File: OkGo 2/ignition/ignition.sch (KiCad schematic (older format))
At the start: 42 parts, among them P101 JST_XH_F, P102 JST_XH_M, P103 CHARGE_CASE, P104 BATT, P105 BATT, P106 SMA, P107 ARM_LED, P108 ARM_LED, SW101 20A ROCKER, U101 CLIP, U102 FUSE 15A, U103 SWD, U104 BEZEL, U105 RFM95W, U106 STM32F071CBT6, U107 TSR 0.5-2433, Y101 8MHz

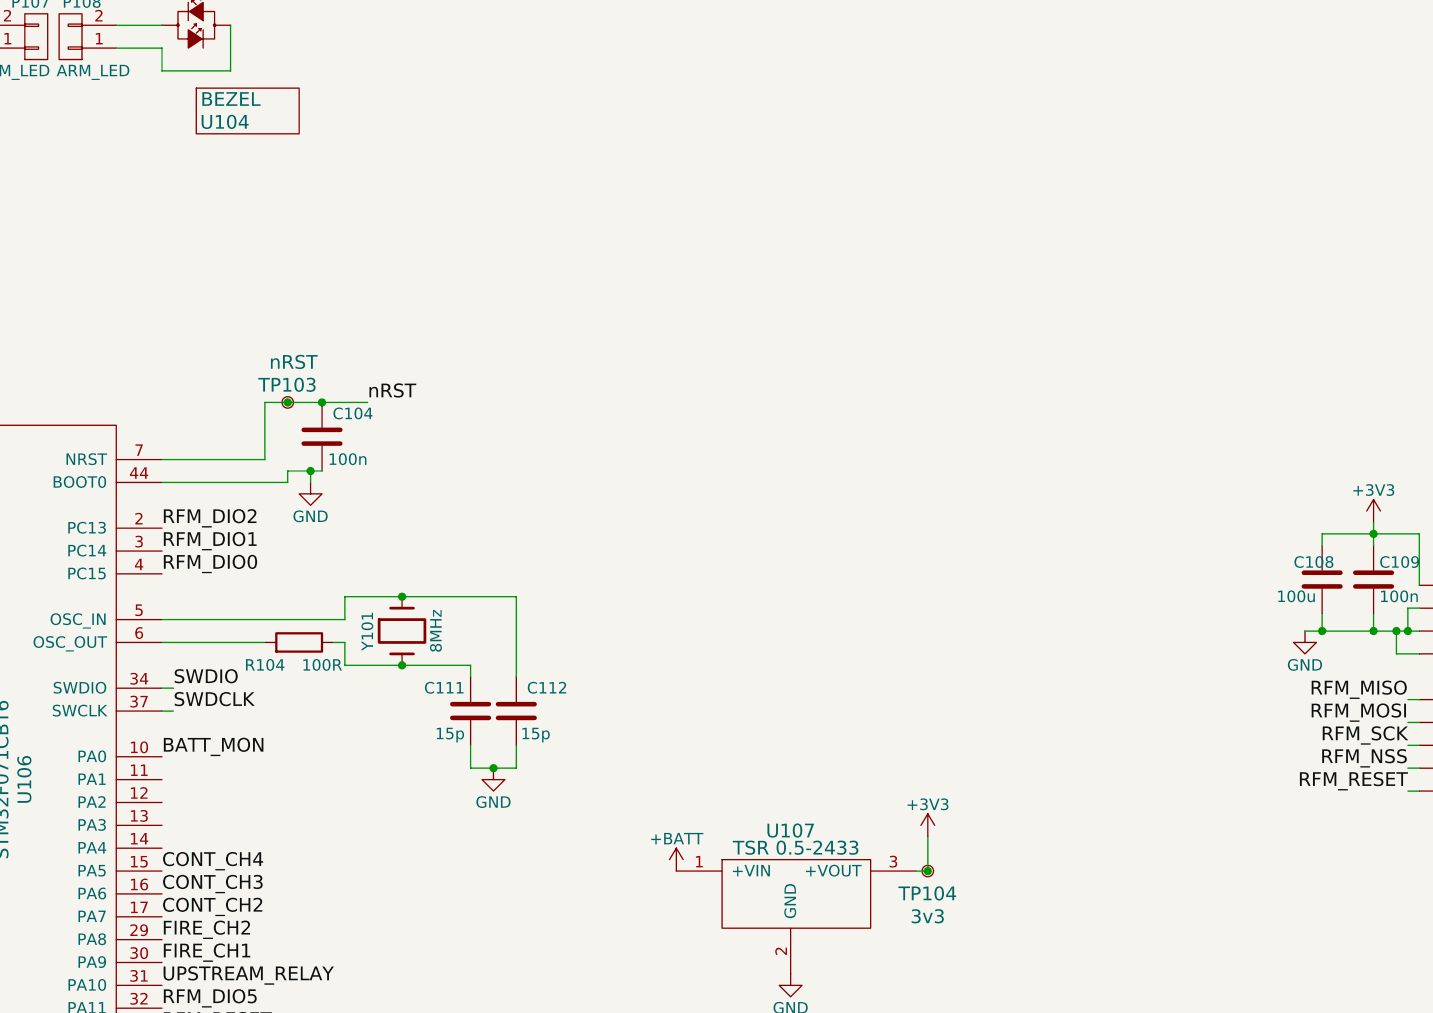
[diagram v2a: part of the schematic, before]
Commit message: Fixed #28, fixed #24, general tidying
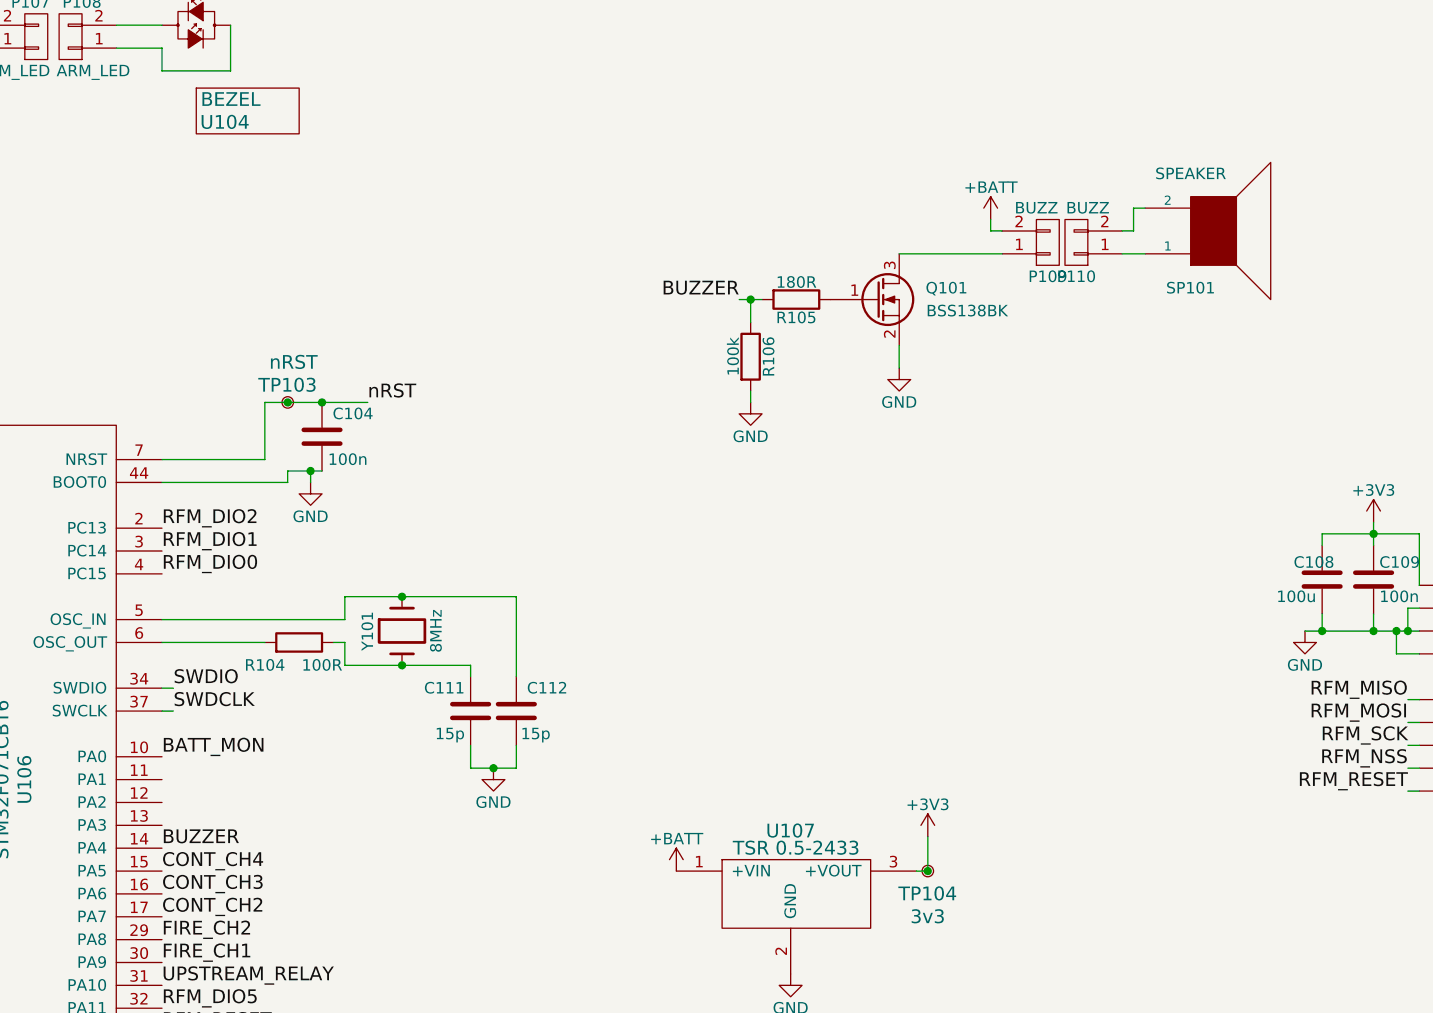
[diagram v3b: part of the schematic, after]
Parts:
- added P109: BUZZ, ignition:JST-PA-2-VERT, symbol CONN_01X02
- added P110: BUZZ, symbol CONN_01X02
- added Q101: BSS138BK, Housings_SOT-23_SOT-143_TSOT-6:SOT-23, symbol Q_NMOS_GSD
- added R105: 180R, Resistors_SMD:R_0805, symbol R
- added R106: 100k, Resistors_SMD:R_0805, symbol R
- added SP101: SPEAKER, symbol SPEAKER
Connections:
- net +BATT: now also P109.2 (P2)
- net GND: now also Q101.2 (S), R106.2
- net BUZZER: now reaches U106.14 (PA4)
- net BUZZER: now also R105.2, R106.1
- new net: P110.1 (P1), SP101.1
- new net: P110.2 (P2), SP101.2
- new net: P109.1 (P1), Q101.3 (D)
- new net: Q101.1 (G), R105.1
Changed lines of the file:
@@
 Wire Wire Line
 	3300 2900 3600 2900
+Text Label 3300 6300 0    60   ~ 0
+BUZZER
+Text Label 5825 3900 2    60   ~ 0
+BUZZER
+$Comp
+L SPEAKER SP101
+U 1 1 55CE427E
+P 7900 3600
+F 0 "SP101" H 7800 3850 50  0000 C CNN
+F 1 "SPEAKER" H 7800 3350 50  0000 C CNN
+F 2 "" H 7900 3600 60  0000 C CNN
+F 3 "http://www.farnell.com/datasheets/1838539.pdf" H 7900 3600 60  0001 C CNN
+F 4 "2433030" H 7900 3600 60  0001 C CNN "Farnell"
+	1    7900 3600
+	1    0    0    1
+$EndComp
+$Comp
+L CONN_01X02 P110
+U 1 1 55CE4BD3
+P 7300 3650
+F 0 "P110" H 7300 3800 50  0000 C CNN
+F 1 "BUZZ" H 7250 3500 50  0000 C CNN
+F 2 "" H 7300 3650 60  0000 C CNN
+F 3 "" H 7300 3650 60  0000 C CNN
+F 4 "1830726" H 7300 3650 60  0001 C CNN "Farnell"
+	1    7300 3650
+	-1   0    0    1
+$EndComp
+Wire Wire Line
+	7500 3700 7600 3700
+Wire Wire Line
+	7500 3600 7550 3600
+Wire Wire Line
+	7550 3600 7550 3500
+Wire Wire Line
+	7550 3500 7600 3500
+$Comp
+L CONN_01X02 P109
+U 1 1 55CE5947
+P 7175 3650
+F 0 "P109" H 7175 3800 50  0000 C CNN
+F 1 "BUZZ" H 7125 3500 50  0000 C CNN
+F 2 "ignition:JST-PA-2-VERT" H 7175 3650 60  0001 C CNN
+F 3 "" H 7175 3650 60  0000 C CNN
+F 4 "1830734" H 7175 3650 60  0001 C CNN "Farnell"
+	1    7175 3650
+	1    0    0    1
+$EndComp
+$Comp
+L +BATT #PWR020
+U 1 1 55CE69CB
+P 6925 3550
+F 0 "#PWR020" H 6925 3400 50  0001 C CNN
+F 1 "+BATT" H 6925 3690 50  0000 C CNN
+F 2 "" H 6925 3550 60  0000 C CNN
+F 3 "" H 6925 3550 60  0000 C CNN
+	1    6925 3550
+	1    0    0    -1
+$EndComp
+Wire Wire Line
+	6925 3550 6925 3600
+Wire Wire Line
+	6925 3600 6975 3600
+$Comp
+L GND #PWR021
+U 1 1 55CEA792
+P 6525 4200
+F 0 "#PWR021" H 6525 3950 50  0001 C CNN
+F 1 "GND" H 6525 4050 50  0000 C CNN
+F 2 "" H 6525 4200 60  0000 C CNN
+F 3 "" H 6525 4200 60  0000 C CNN
+	1    6525 4200
+	1    0    0    -1
+$EndComp
+$Comp
+L R R106
+U 1 1 55CEA799
+P 5875 4150
+F 0 "R106" V 5955 4150 50  0000 C CNN
+F 1 "100k" V 5800 4150 50  0000 C CNN
+F 2 "Resistors_SMD:R_0805" V 5805 4150 30  0001 C CNN
+F 3 "" H 5875 4150 30  0000 C CNN
+F 4 "2331823" H 5875 4150 60  0001 C CNN "Farnell"
+	1    5875 4150
+	1    0    0    -1
+$EndComp
+$Comp
+L GND #PWR022
+U 1 1 55CEA7A0
+P 5875 4350
+F 0 "#PWR022" H 5875 4100 50  0001 C CNN
+F 1 "GND" H 5875 4200 50  0000 C CNN
+F 2 "" H 5875 4350 60  0000 C CNN
+F 3 "" H 5875 4350 60  0000 C CNN
+	1    5875 4350
+	1    0    0    -1
+$EndComp
+$Comp
+L R R105
+U 1 1 55CEA7A7
+P 6075 3900
+F 0 "R105" V 6155 3900 50  0000 C CNN
+F 1 "180R" V 6000 3900 50  0000 C CNN
+F 2 "Resistors_SMD:R_0805" V 6005 3900 30  0001 C CNN
+F 3 "" H 6075 3900 30  0000 C CNN
+F 4 "2331786" H 6075 3900 60  0001 C CNN "Farnell"
+	1    6075 3900
+	0    1    1    0
+$EndComp
+Wire Wire Line
+	6525 4200 6525 4100
+Wire Wire Line
+	5825 3900 5925 3900
+Wire Wire Line
+	5875 4300 5875 4350
+Wire Wire Line
+	5875 3900 5875 4000
+Connection ~ 5875 3900
+$Comp
+L Q_NMOS_GSD Q101
+U 1 1 55CEA7B5
+P 6425 3900
+F 0 "Q101" H 6825 3950 50  0000 R CNN
+F 1 "BSS138BK" H 7000 3850 50  0000 R CNN
+F 2 "Housings_SOT-23_SOT-143_TSOT-6:SOT-23" H 6625 4000 29  0001 C CNN
+F 3 "http://www.farnell.com/datasheets/1455134.pdf" H 6425 3900 60  0001 C CNN
+F 4 "2053833" H 6425 3900 60  0001 C CNN "Farnell"
+	1    6425 3900
+	1    0    0    -1
+$EndComp
+Wire Wire Line
+	6975 3700 6525 3700
 $EndSCHEMATC

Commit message: Changed SMA-F part
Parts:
- P106: Farnell 1608592 -> 1342651
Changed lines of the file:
@@
 F 2 "common:SMA-142-0701-801" H 10525 6050 60  0001 C CNN
 F 3 "" H 10525 6050 60  0000 C CNN
-F 4 "1608592" H 10525 6050 60  0001 C CNN "Farnell"
+F 4 "1342651" H 10525 6050 60  0001 C CNN "Farnell"
 	1    10525 6050
 	1    0    0    -1

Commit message: Corrected a bunch of footprints, see #9
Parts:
- U106: footprint Housings_QFP:LQFP-48_7x7mm_Pitch0.5mm -> common:LQFP48_ST
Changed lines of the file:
@@
 F 0 "U106" V 2700 6300 60  0000 C CNN
 F 1 "STM32F071CBT6" V 2600 6300 60  0000 C CNN
-F 2 "Housings_QFP:LQFP-48_7x7mm_Pitch0.5mm" H 2650 6350 60  0001 C CNN
+F 2 "common:LQFP48_ST" H 2650 6350 60  0001 C CNN
 F 3 "http://www.st.com/st-web-ui/static/active/en/resource/technical/document/datasheet/DM00098745.pdf" H 2650 6350 60  0001 C CNN
 F 4 "2432093" H 2650 6150 60  0001 C CNN "Farnell"
@@
 F 1 "6.3x32" H 4100 1200 50  0000 C CNN
 F 2 "ignition:6x32_fuseclip" H 4225 1250 60  0001 C CNN
-F 3 "" H 4225 1250 60  0000 C CNN
+F 3 "http://www.littelfuse.com/~/media/electronics/datasheets/fuse_clips/littelfuse_fuse_clip_102_122_datasheet.pdf.pdf" H 4225 1250 60  0001 C CNN
 F 4 "1603990" H 4225 1250 60  0001 C CNN "Farnell"
 	1    4225 1250

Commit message: More footprints, partial #9
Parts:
- U105: Farnell (none) -> RF00490
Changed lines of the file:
@@
 F 1 "RFM95W" V 9350 5550 60  0000 C CNN
 F 2 "common:RFM95W" H 9400 5600 60  0001 C CNN
-F 3 "" H 9400 5600 60  0000 C CNN
+F 3 "http://www.farnell.com/datasheets/1870822.pdf" H 9400 5600 60  0001 C CNN
+F 4 "RF00490" H 9400 5550 60  0001 C CNN "Farnell"
 	1    9400 5550
 	1    0    0    -1

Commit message: Penultimate footprinting, partial #9
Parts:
- added P111: SMA, ignition:SMA_upright, symbol SMA
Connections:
- net GND: now also P111.2 (GND), P111.3 (GND), P111.4 (GND), P111.5 (GND)
- net at D103.1, P106.1 (RF), U105.9 (ANT): now also P111.1 (RF)
- no-connect marks 2 -> 10
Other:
- moved on the sheet: P106
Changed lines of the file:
@@
 $EndDescr
 $Comp
-L PWR_FLAG #FLG01
+L PWR_FLAG #FLG101
 U 1 1 5562BA6E
 P 4900 1200
-F 0 "#FLG01" H 4900 1295 50  0001 C CNN
+F 0 "#FLG101" H 4900 1295 50  0001 C CNN
 F 1 "PWR_FLAG" H 4900 1380 50  0000 C CNN
 F 2 "" H 4900 1200 60  0000 C CNN
@@
 $EndComp
 $Comp
-L PWR_FLAG #FLG02
+L PWR_FLAG #FLG102
 U 1 1 5562BA86
 P 4900 1400
-F 0 "#FLG02" H 4900 1495 50  0001 C CNN
+F 0 "#FLG102" H 4900 1495 50  0001 C CNN
 F 1 "PWR_FLAG" H 4900 1580 50  0000 C CNN
 F 2 "" H 4900 1400 60  0000 C CNN
@@
 $EndComp
 $Comp
-L GND #PWR03
+L GND #PWR105
 U 1 1 5562BBD7
 P 5625 2050
-F 0 "#PWR03" H 5625 1800 50  0001 C CNN
+F 0 "#PWR105" H 5625 1800 50  0001 C CNN
 F 1 "GND" H 5625 1900 50  0000 C CNN
 F 2 "" H 5625 2050 60  0000 C CNN
@@
 $EndComp
 $Comp
-L GND #PWR04
+L GND #PWR120
 U 1 1 5562BDA6
 P 6050 6850
-F 0 "#PWR04" H 6050 6600 50  0001 C CNN
+F 0 "#PWR120" H 6050 6600 50  0001 C CNN
 F 1 "GND" H 6050 6700 50  0000 C CNN
 F 2 "" H 6050 6850 60  0000 C CNN
@@
 $EndComp
 $Comp
-L +3V3 #PWR05
+L +3V3 #PWR116
 U 1 1 5562C50D
 P 6650 6250
-F 0 "#PWR05" H 6650 6100 50  0001 C CNN
+F 0 "#PWR116" H 6650 6100 50  0001 C CNN
 F 1 "+3V3" H 6650 6390 50  0000 C CNN
 F 2 "" H 6650 6250 60  0000 C CNN
@@
 $EndComp
 $Comp
-L +3V3 #PWR06
+L +3V3 #PWR101
 U 1 1 5562CAD0
 P 9250 1100
-F 0 "#PWR06" H 9250 950 50  0001 C CNN
+F 0 "#PWR101" H 9250 950 50  0001 C CNN
 F 1 "+3V3" H 9250 1240 50  0000 C CNN
 F 2 "" H 9250 1100 60  0000 C CNN
@@
 $EndComp
 $Comp
-L GND #PWR07
+L GND #PWR104
 U 1 1 5562CB22
 P 9250 1600
-F 0 "#PWR07" H 9250 1350 50  0001 C CNN
+F 0 "#PWR104" H 9250 1350 50  0001 C CNN
 F 1 "GND" H 9250 1450 50  0000 C CNN
 F 2 "" H 9250 1600 60  0000 C CNN
@@
 NoConn ~ 10550 1450
 $Comp
-L +3V3 #PWR08
+L +3V3 #PWR112
 U 1 1 5562D38F
 P 8600 4875
-F 0 "#PWR08" H 8600 4725 50  0001 C CNN
+F 0 "#PWR112" H 8600 4725 50  0001 C CNN
 F 1 "+3V3" H 8600 5015 50  0000 C CNN
 F 2 "" H 8600 4875 60  0000 C CNN
@@
 $EndComp
 $Comp
-L GND #PWR09
+L GND #PWR113
 U 1 1 5562D3AE
 P 8300 5350
-F 0 "#PWR09" H 8300 5100 50  0001 C CNN
+F 0 "#PWR113" H 8300 5100 50  0001 C CNN
 F 1 "GND" H 8300 5200 50  0000 C CNN
 F 2 "" H 8300 5350 60  0000 C CNN
@@
 $EndComp
 $Comp
-L GND #PWR010
-U 1 1 5562DF61
-P 10275 6300
-F 0 "#PWR010" H 10275 6050 50  0001 C CNN
-F 1 "GND" H 10275 6150 50  0000 C CNN
-F 2 "" H 10275 6300 60  0000 C CNN
-F 3 "" H 10275 6300 60  0000 C CNN
-	1    10275 6300
-	1    0    0    -1
-$EndComp
-$Comp
-L +3V3 #PWR011
+L +3V3 #PWR107
 U 1 1 5562E586
 P 1450 3950
-F 0 "#PWR011" H 1450 3800 50  0001 C CNN
+F 0 "#PWR107" H 1450 3800 50  0001 C CNN
 F 1 "+3V3" H 1450 4090 50  0000 C CNN
 F 2 "" H 1450 3950 60  0000 C CNN
@@
 $EndComp
 $Comp
-L GND #PWR012
+L GND #PWR114
 U 1 1 5562F2E9
 P 1500 5500
-F 0 "#PWR012" H 1500 5250 50  0001 C CNN
+F 0 "#PWR114" H 1500 5250 50  0001 C CNN
 F 1 "GND" H 1500 5350 50  0000 C CNN
 F 2 "" H 1500 5500 60  0000 C CNN
@@
 $EndComp
 $Comp
-L GND #PWR013
+L GND #PWR111
 U 1 1 5562F9AC
 P 3950 4700
-F 0 "#PWR013" H 3950 4450 50  0001 C CNN
+F 0 "#PWR111" H 3950 4450 50  0001 C CNN
 F 1 "GND" H 3950 4550 50  0000 C CNN
 F 2 "" H 3950 4700 60  0000 C CNN
@@
 $EndComp
 $Comp
-L GND #PWR014
+L GND #PWR115
 U 1 1 5563121C
 P 4750 5950
-F 0 "#PWR014" H 4750 5700 50  0001 C CNN
+F 0 "#PWR115" H 4750 5700 50  0001 C CNN
 F 1 "GND" H 4750 5800 50  0000 C CNN
 F 2 "" H 4750 5950 60  0000 C CNN
@@
 Bat: 3*4.2V\nMon: 3.1V
 $Comp
-L +3V3 #PWR015
+L +3V3 #PWR110
 U 1 1 559CAD6D
 P 1900 4500
-F 0 "#PWR015" H 1900 4350 50  0001 C CNN
+F 0 "#PWR110" H 1900 4350 50  0001 C CNN
 F 1 "+3V3" H 1900 4640 50  0000 C CNN
 F 2 "" H 1900 4500 60  0000 C CNN
@@
 L SMA P106
 U 1 1 559E7125
-P 10525 6050
-F 0 "P106" H 10625 5950 60  0000 C CNN
-F 1 "SMA" H 10625 6150 60  0000 C CNN
-F 2 "common:SMA-142-0701-801" H 10525 6050 60  0001 C CNN
-F 3 "" H 10525 6050 60  0000 C CNN
-F 4 "1342651" H 10525 6050 60  0001 C CNN "Farnell"
-	1    10525 6050
-	1    0    0    -1
-$EndComp
-$Comp
-L GND #PWR016
+P 10600 6200
+F 0 "P106" H 10700 6100 60  0000 C CNN
+F 1 "SMA" H 10700 6300 60  0000 C CNN
+F 2 "common:SMA-142-0701-801" H 10600 6200 60  0001 C CNN
+F 3 "" H 10600 6200 60  0000 C CNN
+F 4 "1342651" H 10600 6200 60  0001 C CNN "Farnell"
+	1    10600 6200
+	1    0    0    -1
+$EndComp
+$Comp
+L GND #PWR118
 U 1 1 559E749A
-P 10375 5850
-F 0 "#PWR016" H 10375 5600 50  0001 C CNN
-F 1 "GND" H 10375 5700 50  0001 C CNN
-F 2 "" H 10375 5850 60  0000 C CNN
-F 3 "" H 10375 5850 60  0000 C CNN
-	1    10375 5850
-	-1   0    0    1
+P 10475 6375
+F 0 "#PWR118" H 10475 6125 50  0001 C CNN
+F 1 "GND" H 10475 6225 50  0001 C CNN
+F 2 "" H 10475 6375 60  0000 C CNN
+F 3 "" H 10475 6375 60  0000 C CNN
+	1    10475 6375
+	1    0    0    -1
 $EndComp
 $Comp
@@
 $EndComp
 $Comp
-L GND #PWR017
+L GND #PWR103
 U 1 1 55A1A3D6
 P 5425 1400
-F 0 "#PWR017" H 5425 1150 50  0001 C CNN
+F 0 "#PWR103" H 5425 1150 50  0001 C CNN
 F 1 "GND" H 5425 1250 50  0000 C CNN
 F 2 "" H 5425 1400 60  0000 C CNN
@@
 $EndComp
 $Comp
-L +BATT #PWR018
+L +BATT #PWR102
 U 1 1 55A1ACA2
 P 5425 1200
-F 0 "#PWR018" H 5425 1050 50  0001 C CNN
+F 0 "#PWR102" H 5425 1050 50  0001 C CNN
 F 1 "+BATT" H 5425 1340 50  0000 C CNN
 F 2 "" H 5425 1200 60  0000 C CNN
@@
 $EndComp
 $Comp
-L +BATT #PWR019
+L +BATT #PWR119
 U 1 1 55A85387
 P 5550 6400
-F 0 "#PWR019" H 5550 6250 50  0001 C CNN
+F 0 "#PWR119" H 5550 6250 50  0001 C CNN
 F 1 "+BATT" H 5550 6540 50  0000 C CNN
 F 2 "" H 5550 6400 60  0000 C CNN
@@
 Connection ~ 8600 5350
 Wire Wire Line
-	10275 6150 10425 6150
-Wire Wire Line
-	10275 6150 10275 6300
-Wire Wire Line
-	10000 6050 10425 6050
-Wire Wire Line
 	1450 5100 1400 5100
 Wire Wire Line
@@
 Connection ~ 10075 6050
 Wire Wire Line
-	10075 6275 10275 6275
-Connection ~ 10275 6275
-Wire Wire Line
 	9700 2850 9750 2850
 Wire Wire Line
@@
 	1450 4200 1750 4200
 Connection ~ 1450 4200
-Wire Wire Line
-	10350 6150 10350 6200
-Wire Wire Line
-	10350 6200 10425 6200
-Connection ~ 10350 6150
-Wire Wire Line
-	10375 5850 10375 5950
-Wire Wire Line
-	10375 5900 10425 5900
-Wire Wire Line
-	10375 5950 10425 5950
-Connection ~ 10375 5900
 Wire Wire Line
 	5425 1350 5425 1400
@@
 $EndComp
 $Comp
-L +BATT #PWR020
+L +BATT #PWR106
 U 1 1 55CE69CB
 P 6925 3550
-F 0 "#PWR020" H 6925 3400 50  0001 C CNN
+F 0 "#PWR106" H 6925 3400 50  0001 C CNN
 F 1 "+BATT" H 6925 3690 50  0000 C CNN
 F 2 "" H 6925 3550 60  0000 C CNN
@@
 	6925 3600 6975 3600
 $Comp
-L GND #PWR021
+L GND #PWR108
 U 1 1 55CEA792
 P 6525 4200
-F 0 "#PWR021" H 6525 3950 50  0001 C CNN
+F 0 "#PWR108" H 6525 3950 50  0001 C CNN
 F 1 "GND" H 6525 4050 50  0000 C CNN
 F 2 "" H 6525 4200 60  0000 C CNN
@@
 $EndComp
 $Comp
-L GND #PWR022
+L GND #PWR109
 U 1 1 55CEA7A0
 P 5875 4350
-F 0 "#PWR022" H 5875 4100 50  0001 C CNN
+F 0 "#PWR109" H 5875 4100 50  0001 C CNN
 F 1 "GND" H 5875 4200 50  0000 C CNN
 F 2 "" H 5875 4350 60  0000 C CNN
@@
 Wire Wire Line
 	6975 3700 6525 3700
+NoConn ~ 3300 6000
+NoConn ~ 3300 6100
+NoConn ~ 3300 6200
+NoConn ~ 1950 6150
+NoConn ~ 1950 6950
+NoConn ~ 1950 7050
+NoConn ~ 1950 7150
+NoConn ~ 1950 7250
+$Comp
+L SMA P111
+U 1 1 55D3E20E
+P 10600 5850
+F 0 "P111" H 10700 5750 60  0000 C CNN
+F 1 "SMA" H 10700 5950 60  0000 C CNN
+F 2 "ignition:SMA_upright" H 10600 5850 60  0001 C CNN
+F 3 "http://www.farnell.com/cad/1510251.pdf" H 10600 5850 60  0001 C CNN
+F 4 "2144531" H 10600 5850 60  0001 C CNN "Farnell"
+	1    10600 5850
+	1    0    0    -1
+$EndComp
+Wire Wire Line
+	10500 6350 10475 6350
+Wire Wire Line
+	10475 5700 10475 6375
+Wire Wire Line
+	10500 6300 10475 6300
+Connection ~ 10475 6350
+Wire Wire Line
+	10500 6100 10475 6100
+Connection ~ 10475 6300
+Wire Wire Line
+	10500 6050 10475 6050
+Connection ~ 10475 6100
+Wire Wire Line
+	10500 6000 10475 6000
+Connection ~ 10475 6050
+Wire Wire Line
+	10475 5950 10500 5950
+Connection ~ 10475 6000
+Wire Wire Line
+	10500 5750 10475 5750
+Connection ~ 10475 5950
+Wire Wire Line
+	10500 5700 10475 5700
+Connection ~ 10475 5750
+Wire Wire Line
+	10000 6050 10375 6050
+Wire Wire Line
+	10375 5850 10375 6200
+Wire Wire Line
+	10375 6200 10500 6200
+$Comp
+L GND #PWR117
+U 1 1 5562DF61
+P 10075 6275
+F 0 "#PWR117" H 10075 6025 50  0001 C CNN
+F 1 "GND" H 10075 6125 50  0000 C CNN
+F 2 "" H 10075 6275 60  0000 C CNN
+F 3 "" H 10075 6275 60  0000 C CNN
+	1    10075 6275
+	1    0    0    -1
+$EndComp
+Wire Wire Line
+	10500 5850 10375 5850
+Connection ~ 10375 6050
 $EndSCHEMATC
